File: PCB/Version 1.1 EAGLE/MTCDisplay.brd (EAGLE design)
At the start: 135.9 x 87.6 mm, 38 parts, among them IC1 74HC14N, J1 POWER_JACKPTH, U1 ATMEGA328P_PDIP, U2 57PC5FSWITCHCRAFT, U3 57PC5FSWITCHCRAFT, U4 57PC5FSWITCHCRAFT, U5 57PC5FSWITCHCRAFT, U6 MAX7219DIP, Y1 16MHz

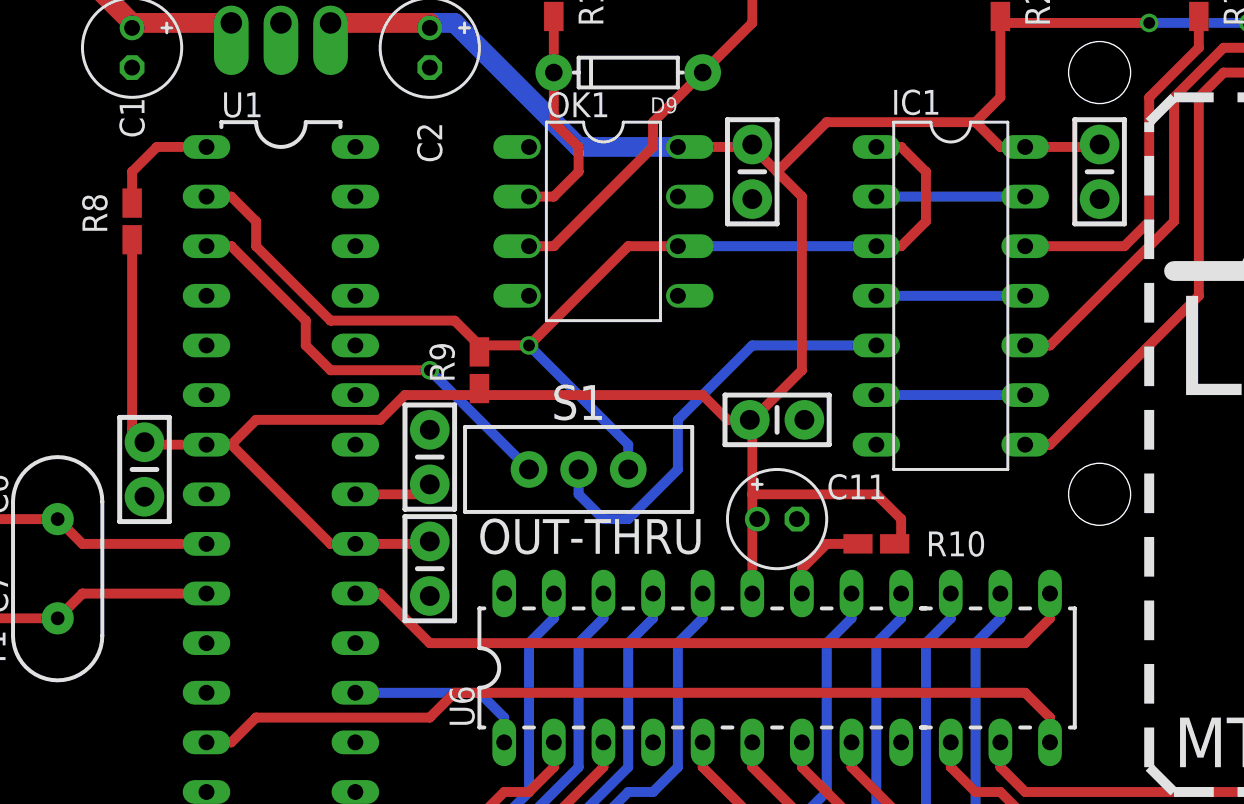
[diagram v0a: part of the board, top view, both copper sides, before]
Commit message: update v1.1 schematics (replace 0.1uF cap package, add part names)
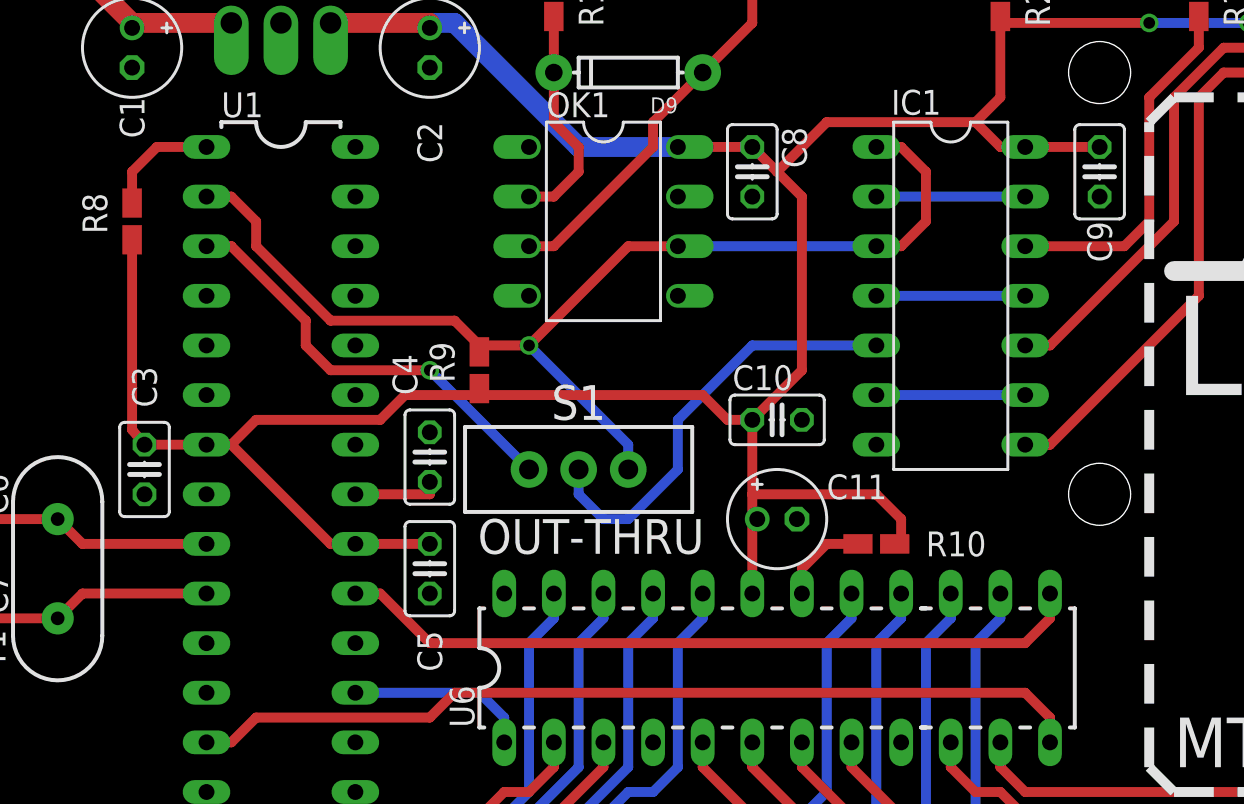
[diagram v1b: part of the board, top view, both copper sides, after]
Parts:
- C10, C3, C4, C5, C8, C9: device SparkFun-Capacitors:CAP-PTH-SMALL-KIT -> rcl:C025-025X050
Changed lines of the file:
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@@
 <setting verticaltext="up"/>
 </settings>
-<grid distance="0.05" unitdist="inch" unit="inch" style="lines" multiple="1" display="yes" altdistance="0.025" altunitdist="inch" altunit="inch"/>
+<grid distance="0.05" unitdist="inch" unit="inch" style="lines" multiple="1" display="no" altdistance="0.025" altunitdist="inch" altunit="inch"/>
 <layers>
 <layer number="1" name="Top" color="4" fill="1" visible="yes" active="yes"/>
@@
 </autorouter>
 <elements>
-<element name="C8" library="SparkFun-Capacitors" package="CAP-PTH-SMALL-KIT" value="0.1uF" x="48.26" y="59.69" rot="R270">
-<attribute name="PROD_ID" value="CAP-08370" x="48.26" y="59.69" size="1.778" layer="27" rot="R270" display="off"/>
-</element>
-<element name="C10" library="SparkFun-Capacitors" package="CAP-PTH-SMALL-KIT" value="0.1uF" x="49.53" y="46.99">
-<attribute name="PROD_ID" value="CAP-08370" x="49.53" y="46.99" size="1.778" layer="27" display="off"/>
-</element>
+<element name="C8" library="rcl" package="C025-025X050" value="0.1uF" x="48.26" y="59.69" rot="R270"/>
+<element name="C10" library="rcl" package="C025-025X050" value="0.1uF" x="49.53" y="46.99"/>
 <element name="C6" library="SparkFun-Capacitors" package="CAP-PTH-SMALL" value="22pF" x="7.62" y="41.91" smashed="yes" rot="R90">
 <attribute name="NAME" x="8.89" y="43.18" size="1.27" layer="25" rot="R90" align="top-center"/>
@@
 <attribute name="VALUE" x="9.144" y="37.084" size="0.4064" layer="27" rot="R90"/>
 </element>
-<element name="C9" library="SparkFun-Capacitors" package="CAP-PTH-SMALL-KIT" value="0.1uF" x="66.04" y="59.69" rot="R270">
-<attribute name="PROD_ID" value="CAP-08370" x="66.04" y="59.69" size="1.778" layer="27" rot="R270" display="off"/>
+<element name="C9" library="rcl" package="C025-025X050" value="0.1uF" x="66.04" y="59.69" smashed="yes" rot="R270">
+<attribute name="NAME" x="66.04" y="57.15" size="1.27" layer="25" ratio="10" rot="R90" align="center-right"/>
+<attribute name="VALUE" x="63.246" y="61.976" size="1.27" layer="27" ratio="10" rot="R270"/>
 </element>
 <element name="D9" library="SparkFun-DiscreteSemi" package="DIODE-1N4148" value="" x="41.91" y="64.77" rot="R180">
@@
 <element name="U4" library="con-switchcraft" package="DIN_5_FEMALE_SUPPORT" value="57PC5FSWITCHCRAFT" x="88.9" y="74.93" rot="R180"/>
 <element name="U5" library="con-switchcraft" package="DIN_5_FEMALE_SUPPORT" value="57PC5FSWITCHCRAFT" x="111.76" y="74.93" rot="R180"/>
-<element name="C3" library="SparkFun-Capacitors" package="CAP-PTH-SMALL-KIT" value="1uF" x="17.145" y="44.45" rot="R270">
-<attribute name="PROD_ID" value="CAP-08370" x="17.145" y="44.45" size="1.778" layer="27" rot="R270" display="off"/>
+<element name="C3" library="rcl" package="C025-025X050" value="1uF" x="17.145" y="44.45" smashed="yes" rot="R270">
+<attribute name="NAME" x="17.145" y="47.625" size="1.27" layer="25" ratio="10" rot="R270" align="center-right"/>
+<attribute name="VALUE" x="14.351" y="46.736" size="1.27" layer="27" ratio="10" rot="R270"/>
 </element>
 <element name="C1" library="resistor" package="E2-5" value="10uF" x="16.51" y="66.04" smashed="yes" rot="R270">
@@
 <attribute name="VALUE" x="29.591" y="63.5" size="1.27" layer="27" ratio="10" rot="R270"/>
 </element>
-<element name="C5" library="SparkFun-Capacitors" package="CAP-PTH-SMALL-KIT" value="0.1uF" x="31.75" y="45.085" rot="R90">
-<attribute name="PROD_ID" value="CAP-08370" x="31.75" y="45.085" size="1.778" layer="27" rot="R90" display="off"/>
+<element name="C5" library="rcl" package="C025-025X050" value="0.1uF" x="31.75" y="45.085" smashed="yes" rot="R90">
+<attribute name="NAME" x="31.75" y="36.195" size="1.27" layer="25" ratio="10" rot="R90" align="center-right"/>
+<attribute name="VALUE" x="34.544" y="42.799" size="1.27" layer="27" ratio="10" rot="R90"/>
 </element>
-<element name="C4" library="SparkFun-Capacitors" package="CAP-PTH-SMALL-KIT" value="0.1uF" x="31.75" y="39.37" rot="R270">
-<attribute name="PROD_ID" value="CAP-08370" x="31.75" y="39.37" size="1.778" layer="27" rot="R270" display="off"/>
+<element name="C4" library="rcl" package="C025-025X050" value="0.1uF" x="31.75" y="39.37" smashed="yes" rot="R270">
+<attribute name="NAME" x="30.48" y="48.26" size="1.27" layer="25" ratio="10" rot="R270" align="center-right"/>
+<attribute name="VALUE" x="28.956" y="41.656" size="1.27" layer="27" ratio="10" rot="R270"/>
 </element>
 <element name="C11" library="resistor" package="E2-5" value="10uF" x="49.53" y="41.91"/>
@@
 <wire x1="20.32" y1="45.72" x2="17.272" y2="45.72" width="0.508" layer="1"/>
 <wire x1="62.23" y1="60.96" x2="65.913" y2="60.96" width="0.508" layer="1"/>
-<wire x1="65.913" y1="60.96" x2="66.04" y2="61.087" width="0.508" layer="1"/>
+<wire x1="65.913" y1="60.96" x2="66.04" y2="60.96" width="0.508" layer="1"/>
 <wire x1="48.26" y1="43.18" x2="54.61" y2="43.18" width="0.508" layer="1"/>
 <wire x1="49.53" y1="59.69" x2="50.8" y2="58.42" width="0.508" layer="1"/>
 <wire x1="50.8" y1="58.42" x2="50.8" y2="49.53" width="0.508" layer="1"/>
 <wire x1="50.8" y1="49.53" x2="48.26" y2="46.99" width="0.508" layer="1"/>
-<wire x1="48.133" y1="46.99" x2="48.26" y2="46.99" width="0.508" layer="1"/>
-<wire x1="48.133" y1="46.99" x2="46.99" y2="46.99" width="0.508" layer="1"/>
+<wire x1="48.26" y1="46.99" x2="46.99" y2="46.99" width="0.508" layer="1"/>
 <wire x1="46.99" y1="46.99" x2="45.72" y2="48.26" width="0.508" layer="1"/>
 <wire x1="45.72" y1="48.26" x2="34.29" y2="48.26" width="0.508" layer="1"/>
@@
 <wire x1="55.88" y1="40.64" x2="55.55" y2="40.64" width="0.508" layer="1"/>
 <wire x1="27.94" y1="40.64" x2="31.75" y2="40.64" width="0.508" layer="1"/>
-<wire x1="31.75" y1="40.64" x2="31.75" y2="40.767" width="0.508" layer="1"/>
 <wire x1="16.51" y1="56.21" x2="16.51" y2="46.482" width="0.508" layer="1"/>
-<wire x1="16.51" y1="46.482" x2="17.145" y2="45.847" width="0.508" layer="1"/>
+<wire x1="16.51" y1="46.482" x2="17.145" y2="45.72" width="0.508" layer="1"/>
 <wire x1="91.44" y1="67.31" x2="83.82" y2="67.31" width="0.508" layer="1"/>
 <wire x1="73.66" y1="67.31" x2="83.82" y2="67.31" width="0.508" layer="1"/>
@@
 <wire x1="62.23" y1="60.96" x2="60.96" y2="60.96" width="0.508" layer="1"/>
 <wire x1="60.96" y1="60.96" x2="59.69" y2="62.23" width="0.508" layer="1"/>
-<wire x1="17.272" y1="45.72" x2="17.145" y2="45.847" width="0.508" layer="1"/>
+<wire x1="17.272" y1="45.72" x2="17.145" y2="45.72" width="0.508" layer="1"/>
 <wire x1="22.86" y1="46.99" x2="21.59" y2="45.72" width="0.508" layer="1"/>
 <contactref element="C11" pad="+"/>
@@
 <wire x1="31.75" y1="67.31" x2="31.75" y2="67.056" width="1.016" layer="16"/>
 <wire x1="44.45" y1="60.96" x2="48.26" y2="60.96" width="0.508" layer="1"/>
-<wire x1="48.26" y1="61.087" x2="48.26" y2="60.96" width="0.508" layer="1"/>
 <wire x1="48.26" y1="60.96" x2="49.53" y2="59.69" width="0.508" layer="1"/>
 <wire x1="49.53" y1="59.69" x2="52.07" y2="62.23" width="0.508" layer="1"/>
@@
 <contactref element="C5" pad="1"/>
 <wire x1="27.94" y1="43.18" x2="31.75" y2="43.18" width="0.508" layer="1"/>
-<wire x1="31.75" y1="43.18" x2="31.75" y2="43.688" width="0.508" layer="1"/>
+<wire x1="31.75" y1="43.18" x2="31.75" y2="43.815" width="0.508" layer="1"/>
 </signal>
 <signal name="UART-TX">

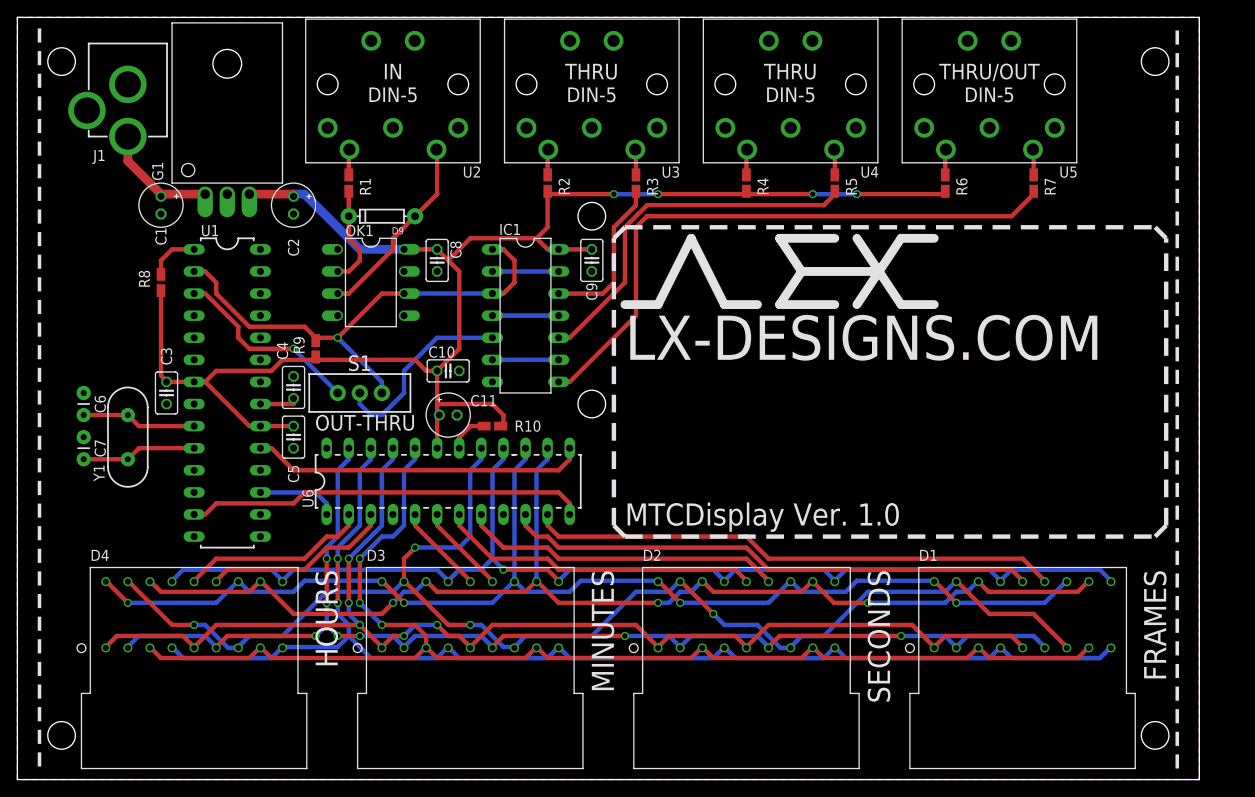
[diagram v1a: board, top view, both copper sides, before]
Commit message: Update segment display package
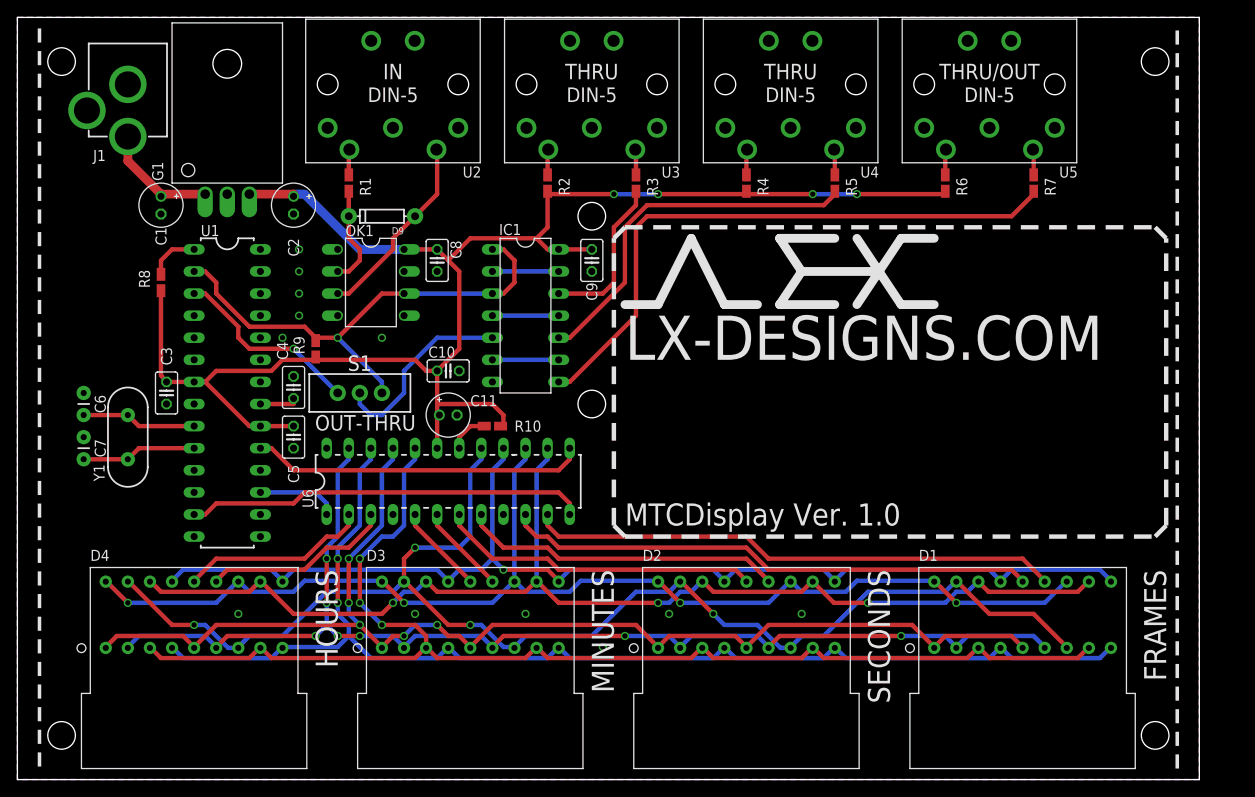
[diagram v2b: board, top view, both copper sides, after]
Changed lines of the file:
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@@
 <setting verticaltext="up"/>
 </settings>
-<grid distance="0.05" unitdist="inch" unit="inch" style="lines" multiple="1" display="no" altdistance="0.025" altunitdist="inch" altunit="inch"/>
+<grid distance="0.05" unitdist="inch" unit="inch" style="lines" multiple="1" display="yes" altdistance="0.025" altunitdist="inch" altunit="inch"/>
 <layers>
 <layer number="1" name="Top" color="4" fill="1" visible="yes" active="yes"/>
@@
 <contactref element="C4" pad="2"/>
 <contactref element="C11" pad="-"/>
+<via x="90.17" y="19.05" extent="1-16" drill="0.6"/>
+<via x="74.93" y="19.05" extent="1-16" drill="0.6"/>
+<via x="58.42" y="19.05" extent="1-16" drill="0.6"/>
+<via x="67.31" y="15.24" extent="1-16" drill="0.6"/>
+<via x="45.72" y="19.05" extent="1-16" drill="0.6"/>
+<via x="25.4" y="19.05" extent="1-16" drill="0.6"/>
+<via x="41.91" y="50.8" extent="1-16" drill="0.6"/>
+<via x="32.385" y="60.96" extent="1-16" drill="0.6"/>
+<via x="32.385" y="58.42" extent="1-16" drill="0.6"/>
+<via x="32.385" y="55.88" extent="1-16" drill="0.6"/>
+<via x="32.385" y="53.34" extent="1-16" drill="0.6"/>
+<via x="30.48" y="50.8" extent="1-16" drill="0.6"/>
+<wire x1="45.72" y1="19.05" x2="43.18" y2="30.48" width="0" layer="19" extent="1-1"/>
 </signal>
 <signal name="+5V">

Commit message: Remove MIDI OUT, replace all TH capacitor with SMD
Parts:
- removed S1: RX-TX, SparkFun-Electromechanical:SWITCH-SPDT
- C1, C11: value 10uF -> 10u; device resistor:E2-5 -> rcl:C0805K
- C10, C4, C5, C8, C9: value 0.1uF -> 0.1u; device rcl:C025-025X050 -> rcl:C0805K
- C2: value 22uF -> 22u; device resistor:E2-5 -> rcl:C0805K
- C3: value 1uF -> 1u; device rcl:C025-025X050 -> rcl:C0805K
- C6, C7: value 22pF -> 22p; device SparkFun-Capacitors:CAP-PTH-SMALL -> rcl:C0805K
- D9: value (none) -> 1N4148
- moved R10 2.69 mm to (52.7, 42.5), turned to 90 degrees
- moved C10 2.54 mm to (49.5, 44.5)
- moved C7 0.90 mm to (8.26, 37.5)
- moved C6 0.90 mm to (8.26, 41.3), turned to 270 degrees
- moved C3 0.63 mm to (16.5, 44.5)
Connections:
- removed net RX/TX: IC1.5, S1.2
- removed net UART-TX: S1.1, U1.3
- net +5V: now also C11.1, C2.1; no longer C11.+, C2.+
- net GND: now also C1.2, C11.2, C2.2; no longer C1.-, C11.-, C2.-
- net N$16: now also C1.1; no longer C1.+
- net UART-RX: now also IC1.5; no longer S1.3
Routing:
- net RX/TX: track 22.2 -> 0.00 mm
- net UART-TX: track 22.0 -> 0.00 mm, vias 1 -> 0
- net UART-RX: track 57.8 -> 56.7 mm, vias 1 -> 0
- net +5V: track 186.1 -> 185.3 mm, vias 4 -> 5
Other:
- board text added: "1"
- board text added: "MTCDisplay Ver. 1.1"
- board text removed: "MTCDisplay Ver. 1.0"
- board text removed: "OUT-THRU"
